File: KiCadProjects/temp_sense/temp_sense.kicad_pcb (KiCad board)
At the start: 2 copper layers, 18.8 x 18.8 mm, 16 parts, among them J1 Screw_Terminal_01x02, J2 Conn_01x03_Pin, J3 Conn_01x02_Pin, U1 ADS1115IDGS, U2 INA827AIDGKR

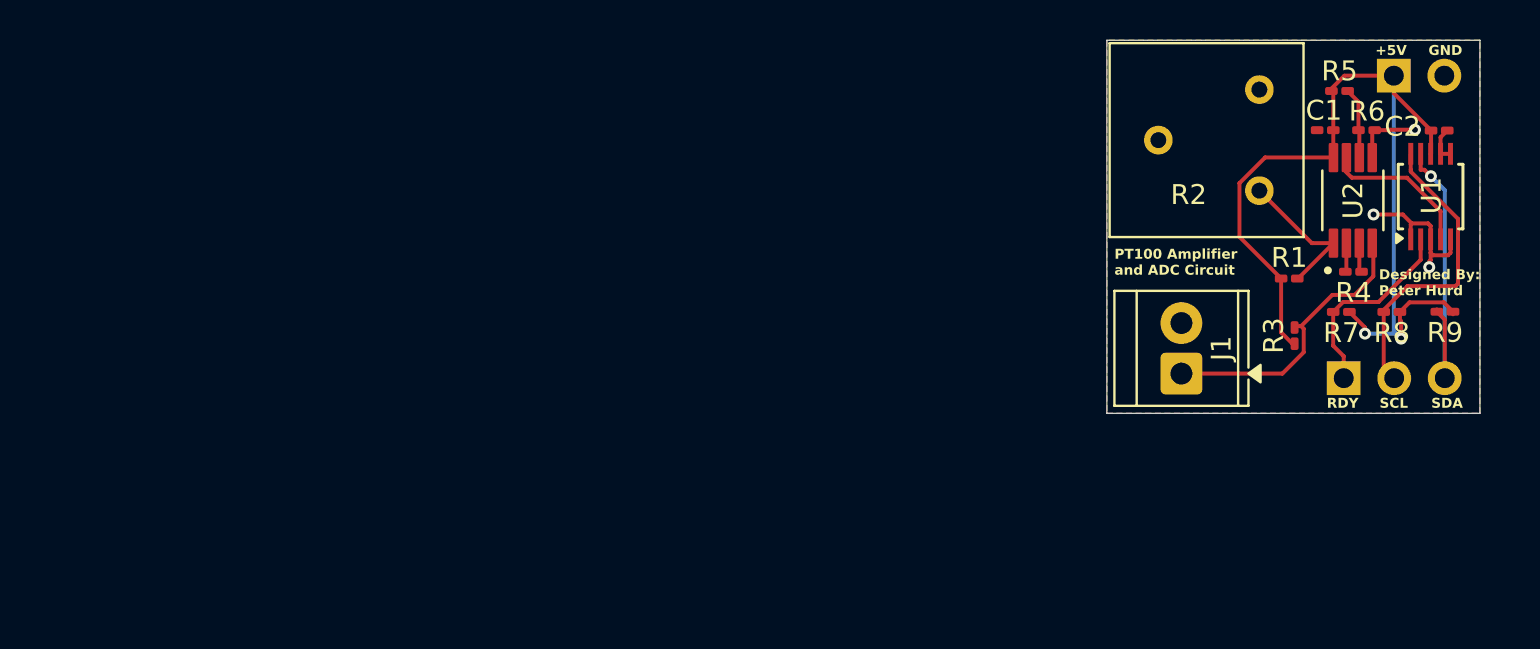
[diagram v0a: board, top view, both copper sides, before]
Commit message: updates to temp circuit
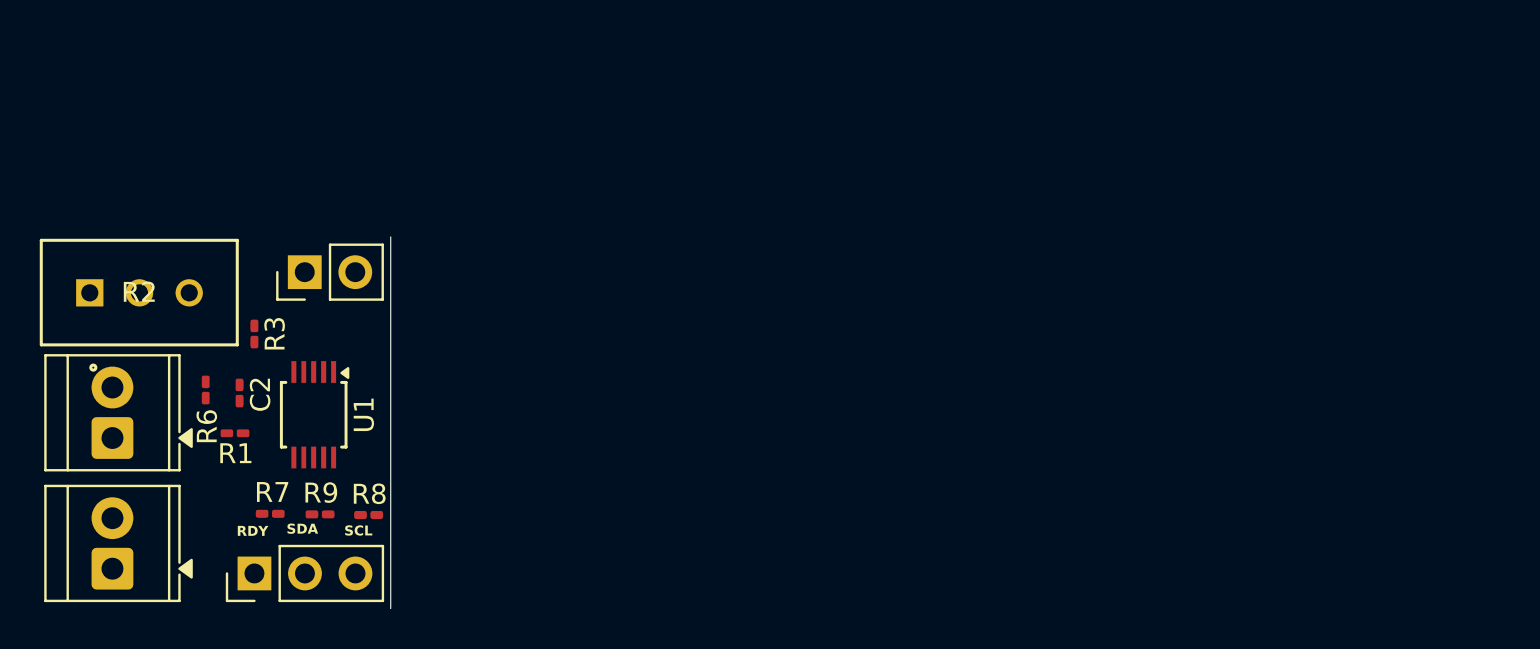
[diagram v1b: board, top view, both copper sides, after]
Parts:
- removed C1: 0.1u, Capacitor_SMD:C_0201_0603Metric_Pad0.64x0.40mm_HandSolder
- removed R4: 5.36k, Resistor_SMD:R_0201_0603Metric_Pad0.64x0.40mm_HandSolder
- removed R5: 10k, Resistor_SMD:R_0201_0603Metric_Pad0.64x0.40mm_HandSolder
- removed U2: INA827AIDGKR, 0_project:SOP65P490X110-8N
- added J4: Conn_01x03_Pin, Connector_PinHeader_2.54mm:PinHeader_1x03_P2.54mm_Vertical, F.Cu at (137.1, 81.8)
- J2: value Conn_01x03_Pin -> Screw_Terminal_01x02; footprint Connector_PinHeader_2.54mm:PinHeader_1x03_P2.54mm_Vertical -> TerminalBlock_TE-Connectivity:TerminalBlock_TE_282834-2_1x02_P2.54mm_Horizontal; moved to F.Cu
- J3: moved to F.Cu
- R1, R3: value 100 -> 1k
- R2: value 100 -> 2k; footprint Potentiometer_THT:Potentiometer_Bourns_3386F_Vertical -> 0_project:POT_PV36W_MUR
- moved J2 62.0 mm to (130.0, 75.0), turned to 90 degrees
- moved C2 61.7 mm to (136.4, 72.7), turned to -90 degrees
- moved R6 59.8 mm to (134.7, 72.6), turned to -90 degrees
- moved R2 59.7 mm to (128.9, 67.7), turned to 0 degrees
- moved R9 57.5 mm to (140.4, 78.8)
- moved U1 57.2 mm to (140.1, 73.8), turned to -90 degrees
- moved J3 55.6 mm to (139.7, 66.7), turned to 90 degrees
- moved R7 54.8 mm to (137.9, 78.8)
- moved J1 54.6 mm to (130.0, 81.6)
- moved R1 53.6 mm to (136.2, 74.8)
- moved R8 52.5 mm to (142.9, 78.9)
- moved R3 52.3 mm to (137.1, 69.8), turned to -90 degrees
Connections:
- J1 pad 1: V+ -> AIN0
- J2 pad 1: ALERT/RDY -> AIN2
- J2 pad 2: SCL -> GND
- R1 pad 2: V- -> AIN-
- R2 pad 3: V- -> AIN-
- R3 pad 2: V+ -> AIN0
- R6 pad 1: Net-(U2-REF) -> +5V
- R6 pad 2: GND -> AIN2
- U1 pad 4: Net-(U1-AIN0) -> AIN0
- U1 pad 5: GND -> AIN-
- U1 pad 6: GND -> AIN2
- U1 pad 7: GND -> AIN-
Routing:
- net +5V: track 47.5 -> 0.00 mm, vias 2 -> 0
- net SDA: track 15.5 -> 0.00 mm, vias 1 -> 0
- net SCL: track 15.4 -> 0.00 mm
- net V+: track 14.7 -> 0.00 mm
- net GND: track 13.1 -> 0.00 mm, vias 3 -> 0
- net ALERT/RDY: track 10.1 -> 0.00 mm
- net Net-(U1-AIN0): track 7.70 -> 0.00 mm
- net V-: track 7.37 -> 0.00 mm
- net Net-(U2-REF): track 3.59 -> 0.00 mm
- net Net-(U2-RG3): track 1.49 -> 0.00 mm
- net Net-(U2-RG2): track 1.46 -> 0.00 mm
- removed copper zone on B.Cu, net GND
- removed copper zone on F.Cu, net GND
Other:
- board outline removed
- board text removed: "+5V"
- board text removed: "Designed By: Peter Hurd"
- board text removed: "GND"
- board text removed: "PT100 Amplifier and ADC Circuit"

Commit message: finish evm board
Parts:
- added C1: 1u, Capacitor_SMD:C_0201_0603Metric_Pad0.64x0.40mm_HandSolder, F.Cu at (115.8, 112.4)
- added C3: 1u, Capacitor_SMD:C_0201_0603Metric_Pad0.64x0.40mm_HandSolder, F.Cu at (115.8, 117.4)
- added J5: VDD Select, Connector_PinHeader_2.54mm:PinHeader_1x03_P2.54mm_Vertical, B.Cu at (119.2, 109.8)
- added J6: AIN1 Select, Connector_PinHeader_2.54mm:PinHeader_1x03_P2.54mm_Vertical, B.Cu at (106.8, 109.8)
- added J7: AIN3 Select, Connector_PinHeader_2.54mm:PinHeader_1x03_P2.54mm_Vertical, B.Cu at (106.8, 130.2)
- added J8: Pull-Up Jumper, Connector_PinHeader_2.54mm:PinHeader_1x02_P2.54mm_Vertical, B.Cu at (101.8, 120.0)
- added J9: ADDR Select, Connector_PinHeader_2.54mm:PinHeader_1x05_P2.54mm_Vertical, B.Cu at (119.2, 120.1)
- added U2: TLV70033_SOT23-5, Package_TO_SOT_SMD:SOT-23-5, F.Cu at (115.5, 114.9)
- J1: value Screw_Terminal_01x02 -> Sensor Input 1
- J2: value Screw_Terminal_01x02 -> Sensor Input 2
- J3: value Conn_01x02_Pin -> Input Header; footprint Connector_PinHeader_2.54mm:PinHeader_1x02_P2.54mm_Vertical -> Connector_PinHeader_2.54mm:PinHeader_1x03_P2.54mm_Vertical
- J4: value Conn_01x03_Pin -> Output Header
- R2: moved to B.Cu
- moved R9 58.6 mm to (108.5, 128.0), turned to 0 degrees
- moved R8 58.2 mm to (111.8, 128.0), turned to 0 degrees
- moved R3 58.1 mm to (106.5, 119.1), turned to 90 degrees
- moved R2 57.8 mm to (110.6, 122.5), turned to 90 degrees
- moved J2 57.6 mm to (103.8, 126.3)
- moved R6 55.9 mm to (106.5, 120.9)
- moved J4 55.3 mm to (110.4, 130.2)
- moved U1 54.5 mm to (115.4, 122.4), turned to 90 degrees
- moved R7 54.3 mm to (115.0, 128.0), turned to 0 degrees
- moved J3 52.2 mm to (110.4, 109.8)
- moved C2 51.1 mm to (114.8, 119.1), turned to 180 degrees
- moved R1 46.4 mm to (108.5, 112.0), turned to 180 degrees
- moved J1 43.5 mm to (103.8, 116.2)
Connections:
- C2 pad 1: +5V -> VDD
- J3 pad 2: GND -> EN
- J4 pad 2: SDA -> SCL
- J4 pad 3: SCL -> SDA
- R1 pad 2: AIN- -> REF
- R2 pad 3: AIN- -> REF
- R3 pad 1: +5V -> Net-(J8-Pin_2)
- R6 pad 1: +5V -> Net-(J8-Pin_2)
- R7 pad 2: ALERT/RDY -> SDA
- R9 pad 2: SDA -> ALERT/RDY
- U1 pad 1: GND -> ADDR
- U1 pad 5: AIN- -> AIN1
- U1 pad 7: AIN- -> AIN3
- U1 pad 8: +5V -> VDD
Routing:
- net +5V: track 0.00 -> 66.6 mm, vias 0 -> 1
- net REF: track 0.00 -> 26.3 mm
- net AIN0: track 0.00 -> 26.3 mm, vias 0 -> 2
- net AIN1: track 0.00 -> 26.0 mm, vias 0 -> 2
- net GND: track 0.00 -> 25.6 mm, vias 0 -> 9
- net VDD: track 0.00 -> 23.2 mm
- net AIN3: track 0.00 -> 21.1 mm
- net AIN2: track 0.00 -> 19.1 mm
- net SCL: track 0.00 -> 18.9 mm
- net ALERT/RDY: track 0.00 -> 15.7 mm, vias 0 -> 2
- net SDA: track 0.00 -> 14.8 mm
- net ADDR: track 0.00 -> 7.54 mm
- net +3.3V: track 0.00 -> 4.71 mm
- net EN: track 0.00 -> 4.70 mm
- net Net-(J8-Pin_2): track 0.00 -> 3.03 mm
- added copper zone on B.Cu, net GND
- added copper zone on F.Cu, net GND
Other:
- board outline added: 21 x 24 mm
- board text added: "+3.3V VDD +5V"
- board text added: "ADS1115 Evaluation Board"
- board text added: "AIN0 GND"
- board text added: "AIN2 GND"
- board text added: "Designed By: Peter Hurd"
- board text added: "GND EN +5V"
- board text added: "Pull-Up"
- board text added: "REF AIN1 GND"
- board text added: "REF AIN3 GND"
- board text added: "SDA SCL RDY"
- board text added: "SDA SCL VDD GND ADDR"
- board text removed: "RDY"
- board text removed: "SCL"
- board text removed: "SDA"

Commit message: temp sense rev 2
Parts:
- removed J7: AIN3 Select, Connector_PinHeader_2.54mm:PinHeader_1x03_P2.54mm_Vertical
- removed J8: Pull-Up Jumper, Connector_PinHeader_2.54mm:PinHeader_1x02_P2.54mm_Vertical
- removed J9: ADDR Select, Connector_PinHeader_2.54mm:PinHeader_1x05_P2.54mm_Vertical
- removed R8, R9: 1k, Resistor_SMD:R_0201_0603Metric_Pad0.64x0.40mm_HandSolder
- added D1: LED, LED_SMD:LED_0603_1608Metric, F.Cu at (226.6, 94.0)
- added D2: LED, LED_SMD:LED_0603_1608Metric, F.Cu at (226.6, 96.5)
- added R4: 1k, Resistor_SMD:R_0603_1608Metric_Pad0.98x0.95mm_HandSolder, F.Cu at (204.0, 100.2)
- added R5: 1k, Resistor_SMD:R_0603_1608Metric_Pad0.98x0.95mm_HandSolder, F.Cu at (204.0, 102.7)
- C1, C2, C3: footprint Capacitor_SMD:C_0201_0603Metric_Pad0.64x0.40mm_HandSolder -> Capacitor_SMD:C_0603_1608Metric_Pad1.08x0.95mm_HandSolder
- J3: value Input Header -> Pull-Up Jumper; footprint Connector_PinHeader_2.54mm:PinHeader_1x03_P2.54mm_Vertical -> Connector_PinHeader_2.54mm:PinHeader_1x02_P2.54mm_Vertical
- J4: value Output Header -> VDD Select
- J5: value VDD Select -> Conn_01x06_Pin; footprint Connector_PinHeader_2.54mm:PinHeader_1x03_P2.54mm_Vertical -> Connector_PinHeader_2.54mm:PinHeader_1x06_P2.54mm_Vertical; moved to F.Cu
- J6: value AIN1 Select -> Conn_01x06_Pin; footprint Connector_PinHeader_2.54mm:PinHeader_1x03_P2.54mm_Vertical -> Connector_PinHeader_2.54mm:PinHeader_1x06_P2.54mm_Vertical; moved to F.Cu
- R1, R3, R6, R7: footprint Resistor_SMD:R_0201_0603Metric_Pad0.64x0.40mm_HandSolder -> Resistor_SMD:R_0603_1608Metric_Pad0.98x0.95mm_HandSolder
- R2: value 2k -> 1k; footprint 0_project:POT_PV36W_MUR -> Resistor_SMD:R_0603_1608Metric_Pad0.98x0.95mm_HandSolder; moved to F.Cu
- moved J2 127.6 mm to (225.5, 88.1), turned to 0 degrees
- moved J1 117.6 mm to (217.9, 88.1), turned to 0 degrees
- moved J4 112.9 mm to (217.7, 95.0), turned to 0 degrees
- moved J3 112.9 mm to (222.3, 95.0), turned to 0 degrees
- moved U1 109.9 mm to (223.4, 102.1), turned to 0 degrees
- moved J6 108.8 mm to (213.1, 86.2), turned to 0 degrees
- moved R3 99.9 mm to (204.0, 97.7), turned to 0 degrees
- moved R6 98.8 mm to (204.0, 105.2), turned to 0 degrees
- moved R1 97.4 mm to (204.0, 92.6), turned to 0 degrees
- moved R2 97.4 mm to (204.0, 95.2), turned to 0 degrees
- moved C2 94.6 mm to (204.0, 87.6), turned to 0 degrees
- moved U2 94.0 mm to (208.8, 103.5), turned to 0 degrees
- moved C1 92.4 mm to (204.0, 85.1), turned to 0 degrees
- moved C3 92.3 mm to (204.0, 90.1), turned to 0 degrees
- moved J5 92.3 mm to (208.5, 86.2), turned to 0 degrees
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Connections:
- J3 pad 2: EN -> Net-(J3-Pin_2)
- J4 pad 1: ALERT/RDY -> +5V
- J4 pad 2: SCL -> VDD
- J4 pad 3: SDA -> +3.3V
- J5 pad 2: VDD -> ADDR
- J5 pad 3: +3.3V -> ALERT/RDY
- J6 pad 1: REF -> +3.3V
- J6 pad 2: AIN1 -> EN
- J6 pad 3: GND -> SCL
- R1 pad 1: +5V -> Net-(J3-Pin_2)
- R1 pad 2: REF -> AIN0
- R2 pad 1: GND -> Net-(J3-Pin_2)
- R2 pad 2: GND -> AIN2
- R3 pad 1: Net-(J8-Pin_2) -> Net-(D1-K)
- R3 pad 2: AIN0 -> GND
- R6 pad 1: Net-(J8-Pin_2) -> +5V
- R6 pad 2: AIN2 -> SDA
- R7 pad 2: SDA -> ALERT/RDY
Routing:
- net +5V: track 66.6 -> 0.00 mm, vias 1 -> 0
- net REF: track 26.3 -> 0.00 mm
- net AIN0: track 26.3 -> 0.00 mm, vias 2 -> 0
- net AIN1: track 26.0 -> 0.00 mm, vias 2 -> 0
- net GND: track 25.6 -> 0.00 mm, vias 9 -> 0
- net VDD: track 23.2 -> 0.00 mm
- net AIN3: track 21.1 -> 0.00 mm
- net AIN2: track 19.1 -> 0.00 mm
- net SCL: track 18.9 -> 0.00 mm
- net ALERT/RDY: track 15.7 -> 0.00 mm, vias 2 -> 0
- net SDA: track 14.8 -> 0.00 mm
- net ADDR: track 7.54 -> 0.00 mm
- net +3.3V: track 4.71 -> 0.00 mm
- net EN: track 4.70 -> 0.00 mm
- net Net-(J8-Pin_2): track 3.03 -> 0.00 mm
- removed copper zone on B.Cu, net GND
- removed copper zone on F.Cu, net GND
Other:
- board outline removed
- board text removed: "+3.3V VDD +5V"
- board text removed: "ADS1115 Evaluation Board"
- board text removed: "AIN0 GND"
- board text removed: "AIN2 GND"
- board text removed: "Designed By: Peter Hurd"
- board text removed: "GND EN +5V"
- board text removed: "Pull-Up"
- board text removed: "REF AIN1 GND"
- board text removed: "REF AIN3 GND"
- board text removed: "SDA SCL RDY"
- board text removed: "SDA SCL VDD GND ADDR"

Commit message: Update ADS1115 Dev board
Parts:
- added G***: LOGO, 0_global:coffee_bean2, B.Cu at (113.0, 100.0)
- J5, J6: moved to B.Cu
- moved J2 123.6 mm to (103.0, 104.9), turned to 90 degrees
- moved J1 115.3 mm to (103.0, 97.7), turned to 90 degrees
- moved J3 113.3 mm to (109.0, 98.7)
- moved U1 110.5 mm to (113.0, 100.0), turned to -90 degrees
- moved D2 106.0 mm to (121.0, 106.0)
- moved D1 105.6 mm to (121.0, 94.0)
- moved J6 98.7 mm to (117.0, 108.9), turned to 90 degrees
- moved R2 95.5 mm to (109.0, 104.5)
- moved R1 95.1 mm to (109.0, 95.5)
- moved J4 94.7 mm to (123.0, 97.5)
- moved R7 94.0 mm to (111.0, 94.0)
- moved C2 92.3 mm to (113.2, 103.9)
- moved J5 91.6 mm to (117.0, 91.1), turned to 90 degrees
- moved U2 89.9 mm to (118.9, 100.0), turned to -90 degrees
- moved R6 88.4 mm to (115.8, 100.0), turned to -90 degrees
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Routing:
- net +5V: track 0.00 -> 45.5 mm
- net VDD: track 0.00 -> 19.4 mm, vias 0 -> 1
- net AIN0: track 0.00 -> 16.4 mm
- net +3.3V: track 0.00 -> 15.5 mm
- net AIN2: track 0.00 -> 15.1 mm
- net SDA: track 0.00 -> 11.7 mm
- net EN: track 0.00 -> 11.5 mm
- net AIN1: track 0.00 -> 10.5 mm, vias 0 -> 1
- net Net-(J3-Pin_2): track 0.00 -> 9.81 mm
- net AIN3: track 0.00 -> 9.34 mm
- net SCL: track 0.00 -> 9.13 mm
- net ALERT/RDY: track 0.00 -> 7.43 mm
- net ADDR: track 0.00 -> 6.89 mm
- net GND: track 0.00 -> 4.69 mm, vias 0 -> 5
- net Net-(D2-K): track 0.00 -> 1.80 mm
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- added copper zone on B.Cu, net GND
- added copper zone on F.Cu, net GND
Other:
- board outline added: 25.5 x 21.3 mm
- board text added: "+3.3V"
- board text added: "+3.3V PWR"
- board text added: "+5V"
- board text added: "+5V PWR"
- board text added: "ADDR"
- board text added: "ADS1115 Dev Board Designed By: Peter H."
- board text added: "AIN0"
- board text added: "AIN1"
- board text added: "AIN2"
- board text added: "AIN3"
- board text added: "ALERT"
- board text added: "EN"
- board text added: "GND"
- board text added: "GND AIN0"
- board text added: "GND AIN2"
- board text added: "Pull-Up Select"
- board text added: "SCL"
- board text added: "SDA"
- board text added: "VDD SELECT"
